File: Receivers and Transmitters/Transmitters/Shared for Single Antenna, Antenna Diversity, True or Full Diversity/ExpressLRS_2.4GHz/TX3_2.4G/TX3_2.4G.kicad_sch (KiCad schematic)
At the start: 12 parts, among them J1 Conn_01x05_Socket, J2 Conn_01x03_Socket, J3 Conn_01x04_Socket, J4 Conn_02x06_Odd_Even, U1 TPS7A4701xRGW, U2 ESP32-WROOM-32, U3 E28-2G4M27S

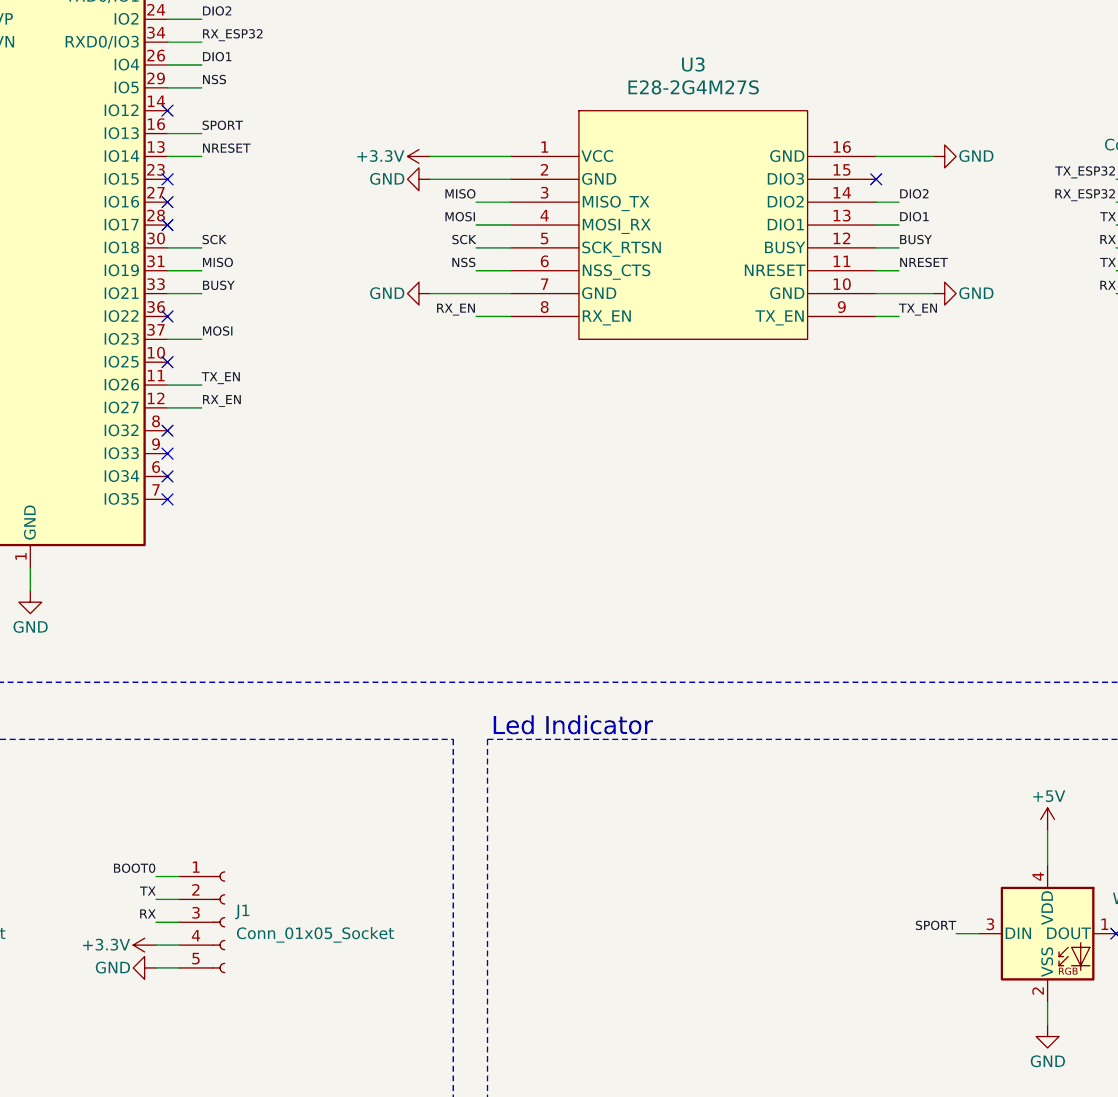
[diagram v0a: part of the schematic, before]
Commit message: Fixed incorrect LED RGB connection to ESP32 on TX2_2.4G and TX3_2.4G schematics and PCBs
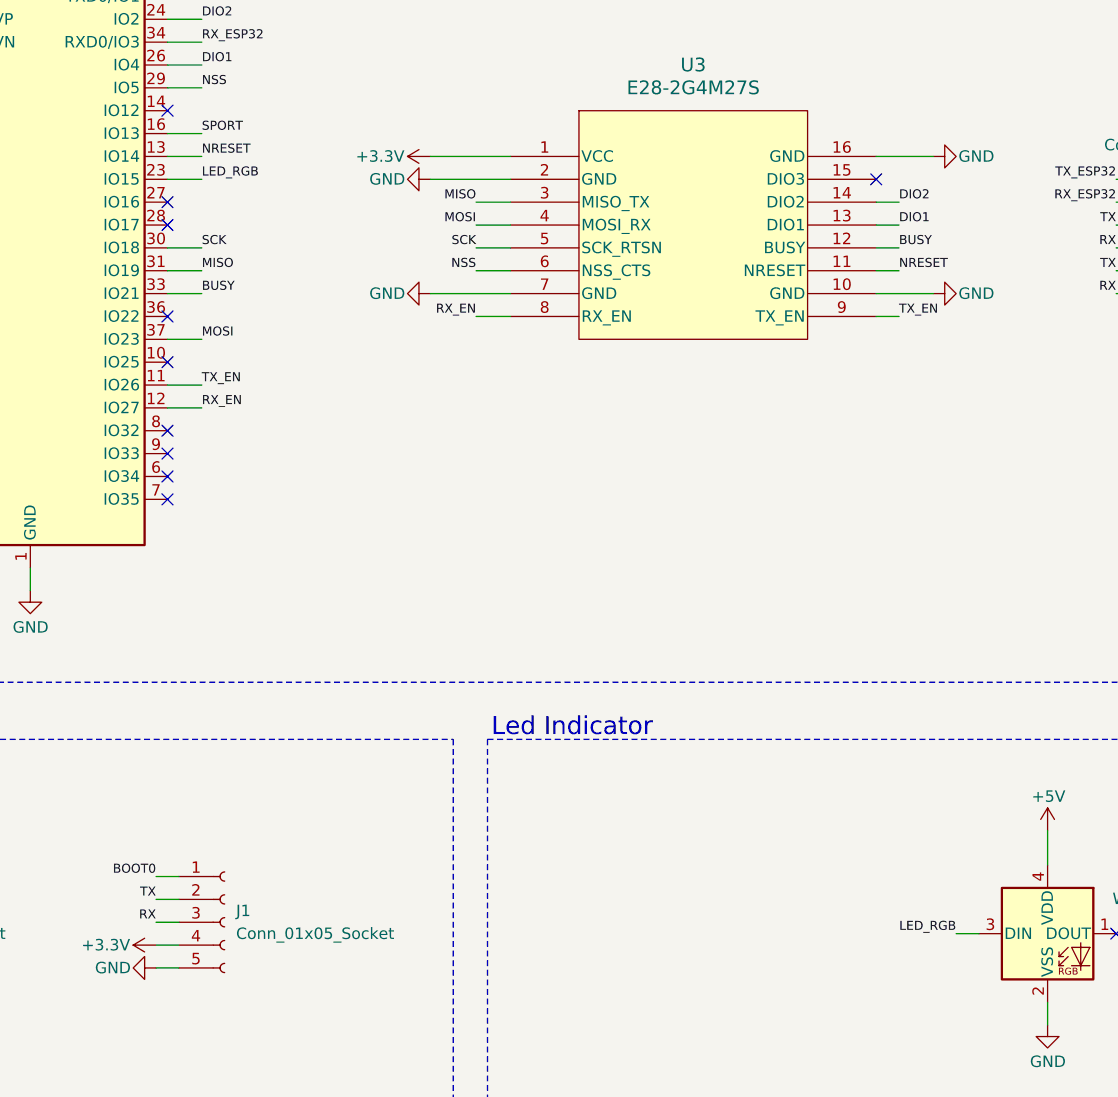
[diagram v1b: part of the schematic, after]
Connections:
- net SPORT: no longer D1.3 (DIN)
- net LED_RGB: now reaches U2.23 (IO15)
- net LED_RGB: now also D1.3 (DIN)
- no-connect marks 25 -> 24
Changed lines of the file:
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@@
-	)
-	(no_connect
-		(at 119.38 58.42)
 	)
 	(no_connect
@@
 	(wire
 		(pts
+			(xy 119.38 58.42) (xy 123.19 58.42)
+		)
+		(stroke
+			(width 0)
+			(type default)
+		)
+	)
+	(wire
+		(pts
 			(xy 242.57 60.96) (xy 251.46 60.96)
 		)
@@
 		)
 	)
+	(label "LED_RGB"
+		(at 123.19 58.42 0)
+		(effects
+			(font
+				(size 1 1)
+			)
+			(justify left bottom)
+		)
+	)
 	(label "DIO2"
 		(at 123.19 40.64 0)
@@
 		)
 	)
-	(label "SPORT"
+	(label "LED_RGB"
 		(at 207.01 142.24 180)
 		(effects
